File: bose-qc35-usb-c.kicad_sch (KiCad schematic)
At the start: 37 parts, among them J1 502426-2030, J2 2171790001, J3 51281-0594, Q1 BC846BM3T5G, U1 TPS25200

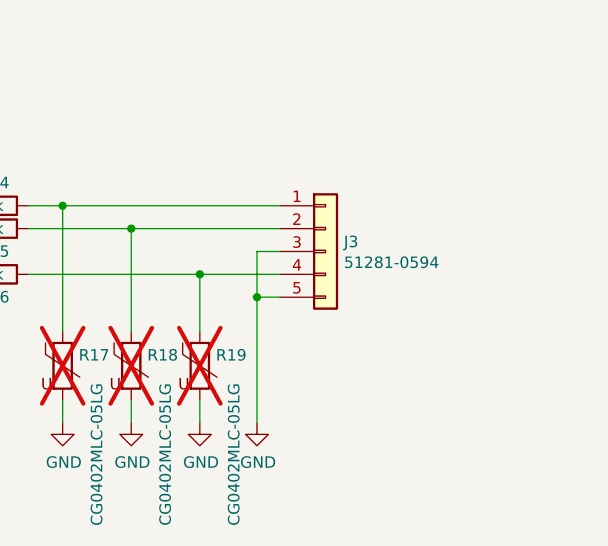
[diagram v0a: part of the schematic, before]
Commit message: Update Molex connector model
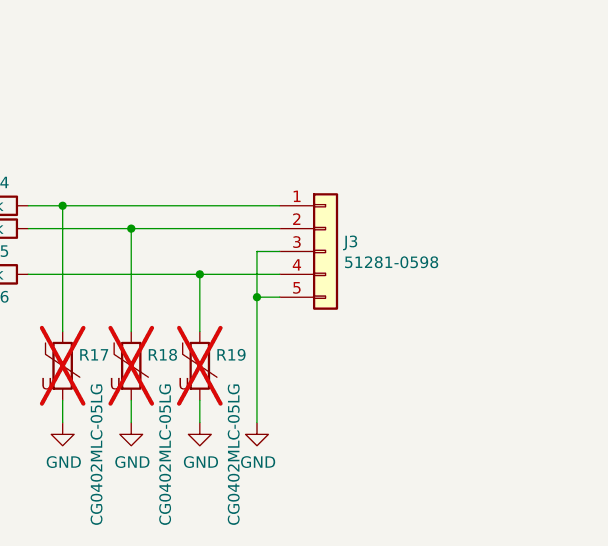
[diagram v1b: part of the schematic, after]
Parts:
- J3: value 51281-0594 -> 51281-0598
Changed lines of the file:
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@@
       (effects (font (size 1.27 1.27)) (justify left))
     )
-    (property "Value" "51281-0594" (at 267.462 48.2346 0)
+    (property "Value" "51281-0598" (at 267.462 48.2346 0)
       (effects (font (size 1.27 1.27)) (justify left))
     )
